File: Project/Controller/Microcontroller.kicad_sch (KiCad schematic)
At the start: 37 parts, among them J2 SWD Connector, J3 USB_C_Receptacle_USB2.0_16P, SW1 SW_SPDT, SW2 SW_SPDT, SW3 SW_Push, U4 STM32F446RCTx, U5 24AA64-OT, U6 USBLC6-2SC6, Y1 25 MHz

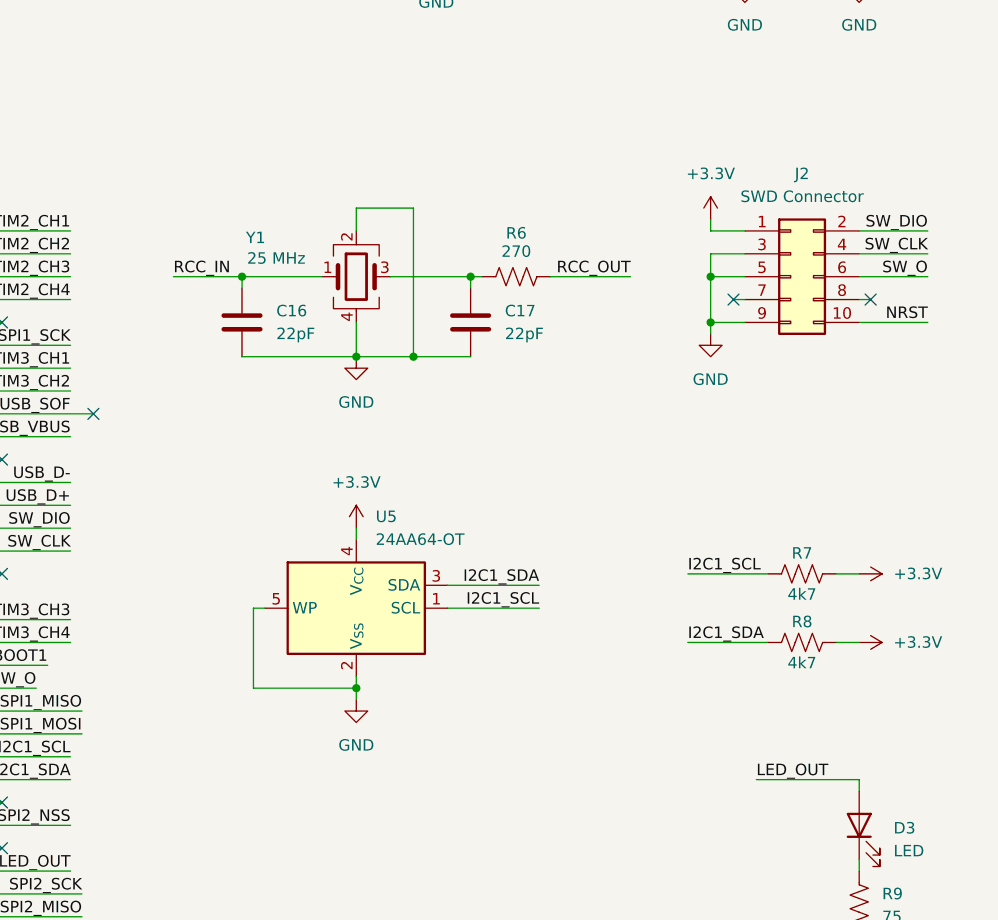
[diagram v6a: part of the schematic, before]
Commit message: Change SWD header to 6 pins
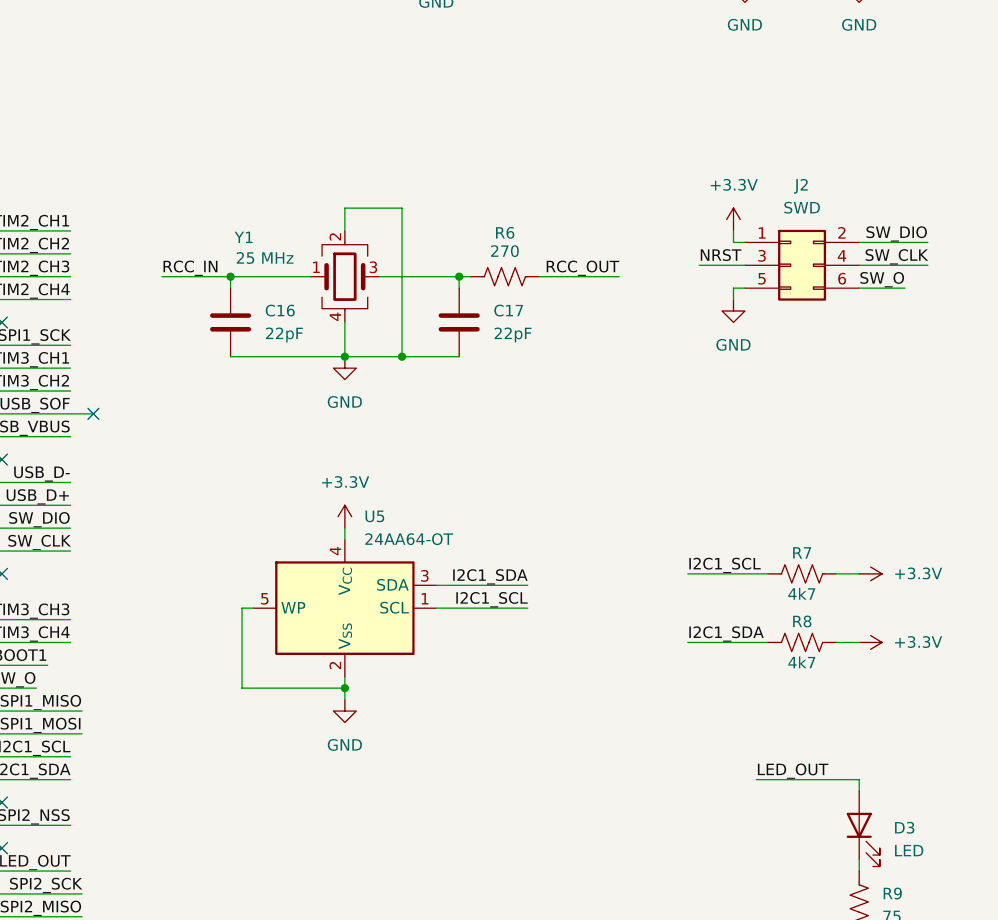
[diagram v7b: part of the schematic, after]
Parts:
- removed J2: SWD Connector, Connector_PinHeader_1.27mm:PinHeader_2x05_P1.27mm_Vertical, symbol Connector_Generic:Conn_02x05_Odd_Even
- added J2: SWD, Connector_PinHeader_2.54mm:PinHeader_2x03_P2.54mm_Vertical, symbol Connector_Generic:Conn_02x03_Odd_Even
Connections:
- net +3.3V: now also J2.1 (Pin_1)
- net GND: now also J2.5 (Pin_5)
- net NRST: now also J2.3 (Pin_3)
- net SW_CLK: now also J2.4 (Pin_4)
- net SW_DIO: now also J2.2 (Pin_2)
- net SW_O: now also J2.6 (Pin_6)
- no-connect marks 12 -> 10
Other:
- moved on the sheet: C16, C17, R6, U5, Y1

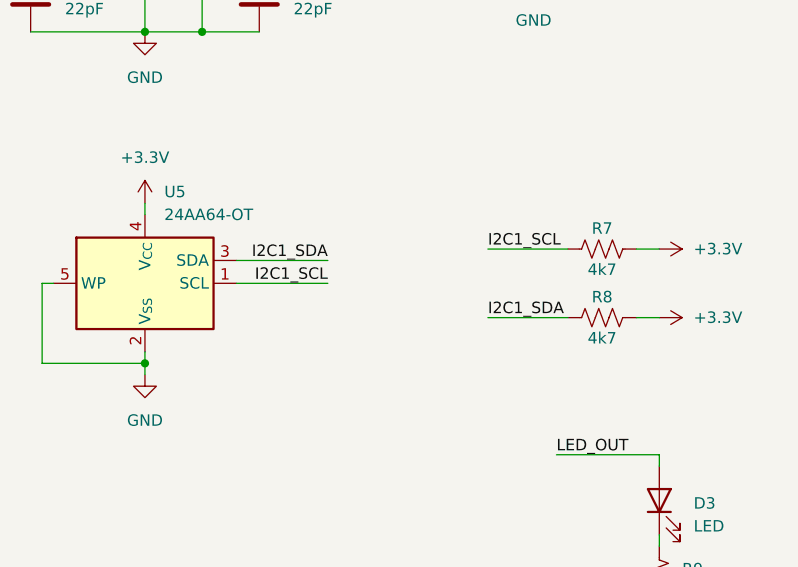
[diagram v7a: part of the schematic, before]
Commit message: Add decoupling capacitor to EEPROM
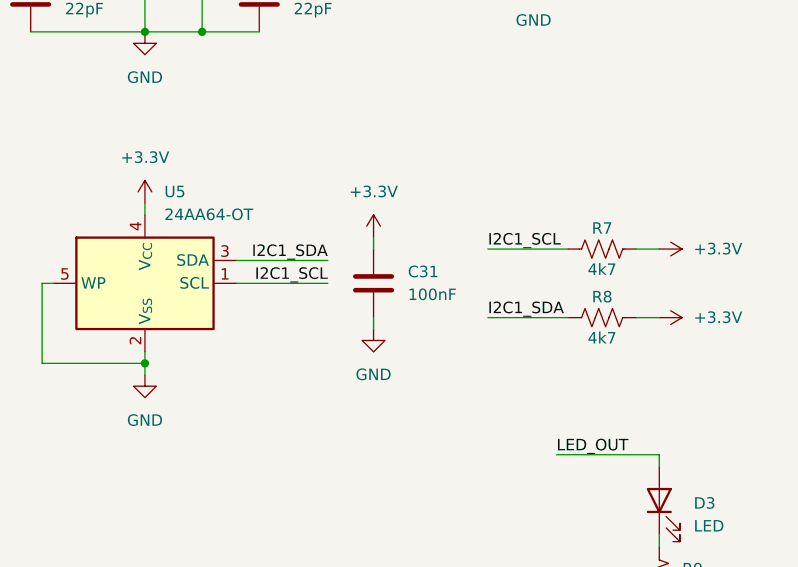
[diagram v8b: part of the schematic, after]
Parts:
- added C31: 100nF, Capacitor_SMD:C_0402_1005Metric, symbol Device:C
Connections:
- net +3.3V: now also C31.1
- net GND: now also C31.2
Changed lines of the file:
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@@
 	(wire
 		(pts
+			(xy 234.95 102.87) (xy 234.95 104.14)
+		)
+		(stroke
+			(width 0)
+			(type default)
+		)
+	)
+	(wire
+		(pts
 			(xy 25.4 36.83) (xy 38.1 36.83)
 		)
@@
 	(wire
 		(pts
+			(xy 234.95 111.76) (xy 234.95 113.03)
+		)
+		(stroke
+			(width 0)
+			(type default)
+		)
+	)
+	(wire
+		(pts
 			(xy 219.71 35.56) (xy 219.71 34.29)
 		)
@@
 	)
 	(symbol
+		(lib_id "power:GND")
+		(at 234.95 113.03 0)
+		(unit 1)
+		(exclude_from_sim no)
+		(in_bom yes)
+		(on_board yes)
+		(dnp no)
+		(fields_autoplaced yes)
+		(property "Reference" "#PWR092"
+			(at 234.95 119.38 0)
+			(effects
+				(font
+					(size 1.27 1.27)
+				)
+				(hide yes)
+			)
+		)
+		(property "Value" "GND"
+			(at 234.95 118.11 0)
+			(effects
+				(font
+					(size 1.27 1.27)
+				)
+			)
+		)
+		(property "Footprint" ""
+			(at 234.95 113.03 0)
+			(effects
+				(font
+					(size 1.27 1.27)
+				)
+				(hide yes)
+			)
+		)
+		(property "Datasheet" ""
+			(at 234.95 113.03 0)
+			(effects
+				(font
+					(size 1.27 1.27)
+				)
+				(hide yes)
+			)
+		)
+		(property "Description" "Power symbol creates a global label with name \"GND\" , ground"
+			(at 234.95 113.03 0)
+			(effects
+				(font
+					(size 1.27 1.27)
+				)
+				(hide yes)
+			)
+		)
+		(pin "1"
+		)
+		(instances
+			(project "XuLabController"
+				(path "/71bb14ae-b730-4d22-a41d-cf68989dae2d/4b34bde8-cf26-4b12-b362-4972fe9ac1d6"
+					(reference "#PWR092")
+					(unit 1)
+				)
+			)
+		)
+	)
+	(symbol
 		(lib_id "power:+3.3V")
 		(at 266.7 104.14 270)
@@
 	)
 	(symbol
+		(lib_id "power:+3.3V")
+		(at 234.95 102.87 0)
+		(unit 1)
+		(exclude_from_sim no)
+		(in_bom yes)
+		(on_board yes)
+		(dnp no)
+		(fields_autoplaced yes)
+		(property "Reference" "#PWR093"
+			(at 234.95 106.68 0)
+			(effects
+				(font
+					(size 1.27 1.27)
+				)
+				(hide yes)
+			)
+		)
+		(property "Value" "+3.3V"
+			(at 234.95 97.79 0)
+			(effects
+				(font
+					(size 1.27 1.27)
+				)
+			)
+		)
+		(property "Footprint" ""
+			(at 234.95 102.87 0)
+			(effects
+				(font
+					(size 1.27 1.27)
+				)
+				(hide yes)
+			)
+		)
+		(property "Datasheet" ""
+			(at 234.95 102.87 0)
+			(effects
+				(font
+					(size 1.27 1.27)
+				)
+				(hide yes)
+			)
+		)
+		(property "Description" "Power symbol creates a global label with name \"+3.3V\""
+			(at 234.95 102.87 0)
+			(effects
+				(font
+					(size 1.27 1.27)
+				)
+				(hide yes)
+			)
+		)
+		(pin "1"
+		)
+		(instances
+			(project "XuLabController"
+				(path "/71bb14ae-b730-4d22-a41d-cf68989dae2d/4b34bde8-cf26-4b12-b362-4972fe9ac1d6"
+					(reference "#PWR093")
+					(unit 1)
+				)
+			)
+		)
+	)
+	(symbol
 		(lib_id "power:GND")
 		(at 209.55 80.01 0)
@@
 					(unit 1)
 				)
+			)
+		)
+	)
+	(symbol
+		(lib_id "Device:C")
+		(at 234.95 107.95 0)
+		(unit 1)
+		(exclude_from_sim no)
+		(in_bom yes)
+		(on_board yes)
+		(dnp no)
+		(fields_autoplaced yes)
+		(property "Reference" "C31"
+			(at 238.76 106.6799 0)
+			(effects
+				(font
+					(size 1.27 1.27)
+				)
+				(justify left)
+			)
+		)
+		(property "Value" "100nF"
+			(at 238.76 109.2199 0)
+			(effects
+				(font
+					(size 1.27 1.27)
+				)
+				(justify left)
+			)
+		)
+		(property "Footprint" "Capacitor_SMD:C_0402_1005Metric"
+			(at 235.9152 111.76 0)
+			(effects
+				(font
+					(size 1.27 1.27)
+				)
+				(hide yes)
+			)
+		)
+		(property "Datasheet" "https://mm.digikey.com/Volume0/opasdata/d220001/medias/docus/503/CL05A104KA5NNNC.pdf"
+			(at 234.95 107.95 0)
+			(effects
+				(font
+					(size 1.27 1.27)
+				)
+				(hide yes)
+			)
+		)
+		(property "Description" "Unpolarized capacitor"
+			(at 234.95 107.95 0)
+			(effects
+				(font
+					(size 1.27 1.27)
+				)
+				(hide yes)
+			)
+		)
+		(property "Listing" "https://www.digikey.com/en/products/detail/samsung-electro-mechanics/CL05A104KA5NNNC/3886701"
+			(at 234.95 107.95 0)
+			(effects
+				(font
+					(size 1.27 1.27)
+				)
+				(hide yes)
+			)
+		)
+		(property "Interchangeable" "Yes"
+			(at 234.95 107.95 0)
+			(effects
+				(font
+					(size 1.27 1.27)
+				)
+				(hide yes)
+			)
+		)
+		(pin "2"
+		)
+		(pin "1"
+		)
+		(instances
+			(project "XuLabController"
+				(path "/71bb14ae-b730-4d22-a41d-cf68989dae2d/4b34bde8-cf26-4b12-b362-4972fe9ac1d6"
+					(reference "C31")
+					(unit 1)
+				)
